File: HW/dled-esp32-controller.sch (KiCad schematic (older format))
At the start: 40 parts, among them J1 PinsI2C, J2 PinsDbg, J3 BootBtn, J4 swRes, J5 LEDcmd, J6 PinsExt, J7 PinsExt2, J8 LEDpwr, J9 Power5V, Q1 STD46P4LLF6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

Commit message: Updates components to add manufacturer, part number, ... fields, checked the values and adds power flags for a clean ERC test
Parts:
- C1, C2, C4, C5, C6, C9: symbol Device:C -> calin:C; characteristics (none) -> 100 nF / 50V / X7R; manufacturer (none) -> Samsung; package (none) -> 0805; part-number (none) -> CL21B104KBCNNNC
- C3: symbol Device:C -> calin:C; characteristics (none) -> 10 µF / 6,3 V; manufacturer (none) -> Samsung; package (none) -> 0805; part-number (none) -> CL21B106KQQNNNE
- C7: value 10uF -> 10uF/10V/1mOhm; symbol Device:C -> calin:C; characteristics (none) -> 10 µF / 16 V / X7R / ESR: 1 mΩ; manufacturer (none) -> Taiyo Yuden; package (none) -> 0805; part-number (none) -> EMK212BB7106KG-T
- C8: value 22uF 1mOhm -> 22uF/6.3V/1mOhm; symbol Device:C -> calin:C; characteristics (none) -> 22 µF / 6.3 V / X5R / ESR: 1 mΩ; manufacturer (none) -> Taiyo Yuden; package (none) -> 0805; part-number (none) -> JMK212BJ226MG-T
- D1: characteristics (none) -> *; manufacturer (none) -> Optoflash; package (none) -> 1206; part-number (none) -> OF-SMD3216B
- H1, H2: characteristics (none) -> *; manufacturer (none) -> pcb; part-number (none) -> DNP
- J1: value PinsI2C -> CS_4
- J2: value PinsDbg -> CS_3
- J3: value BootBtn -> CS_2
- J4: value swRes -> CS_2
- J5: value LEDcmd -> CS_3
- J6: value PinsExt -> CS_5; part-number (none) -> DNP
- J7: value PinsExt2 -> CS_3; part-number (none) -> DNP
- J8: value LEDpwr -> CS_Pwr
- J9: value Power5V -> CS_Pwr; symbol calin:CS_2pwr -> calin:CS_2
- L1: characteristics (none) -> 2.2 uH DCR: 35 mΩ; manufacturer (none) -> Abracon Corporation; package (none) -> *; part-number (none) -> ASPI-0530HI-2R2M-T2
- Q1: characteristics (none) -> *; manufacturer (none) -> STMicroelectronics; package (none) -> DPAK (TO-252); part-number (none) -> STD46P4LLF6
- Q2: characteristics (none) -> *; manufacturer (none) -> International Rectifier; package (none) -> SOT23-3; part-number (none) -> IRLML2502GPbF
- R1: characteristics (none) -> *; manufacturer (none) -> Vishay; package (none) -> 0805; part-number (none) -> CRCW080510K0FKEA
- R10, R2, R5, R9: characteristics (none) -> *; manufacturer (none) -> Vishay; package (none) -> 0805; part-number (none) -> CRCW0805330RFKTABC
- R3, R4: value 2K2 -> 2k2; characteristics (none) -> 2K; manufacturer (none) -> Panasonic; package (none) -> 0805; part-number (none) -> ERJ6ENF2001V
- R6: characteristics (none) -> 442Kohms 1%; manufacturer (none) -> Panasonic; package (none) -> 0805; part-number (none) -> ERJ-6ENF4423V
- R7: characteristics (none) -> 100Kohms 1%; manufacturer (none) -> Panasonic; package (none) -> 0805; part-number (none) -> ERJ-6ENF1003V
- R8: value 10K -> 10k; characteristics (none) -> *; manufacturer (none) -> Vishay; package (none) -> 0805; part-number (none) -> CRCW080510K0FKEA
- SYM1: manufacturer (none) -> pcb; part-number (none) -> DNP
- U1: characteristics (none) -> *; manufacturer (none) -> Espressif; package (none) -> *; part-number (none) -> ESP32-WROOM-32
- U2: characteristics (none) -> Standard CMOS Voltage Detector IC - Open Drain; manufacturer (none) -> ROHM Semiconductor; package (none) -> SSOP3 (SOT23-3); part-number (none) -> BD48K
- U3: characteristics (none) -> Step-Down Converter 2A 1.5MHz Iq=35uA; manufacturer (none) -> Texas Instruments; package (none) -> SOT23-5; part-number (none) -> TLV62569DBV
- U4, U5: characteristics (none) -> Single Power Supply Single Buffer GATE CMOS Logic Level Shi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; manufacturer (none) -> Texas Instruments; package (none) -> SOT23-5; part-number (none) -> SN74LV1T34DBVR
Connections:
- wire segments 126 -> 133
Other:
- moved on the sheet: C6, C7

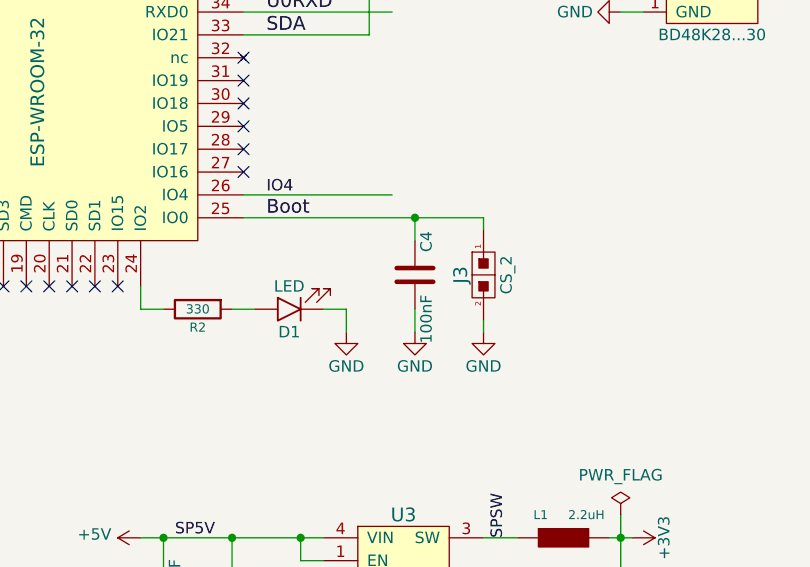
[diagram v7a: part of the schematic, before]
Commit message: Changes the C4 to NC and removes the keepout areas from under ESP32 module, as in Espressif's DevKitC v4
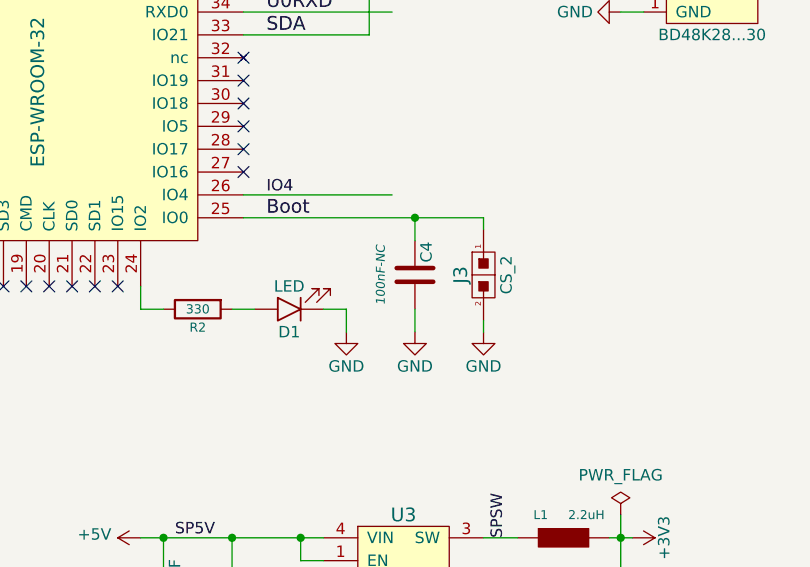
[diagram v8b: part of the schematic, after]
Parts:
- C4: value 100nF -> 100nF-NC; characteristics 100 nF / 50V / X7R -> *; manufacturer Samsung -> (none); part-number CL21B104KBCNNNC -> DNP
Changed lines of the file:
@@
 Sheet 1 1
 Title "dled-esp32-controller"
-Date "2019-04-30"
-Rev "14"
+Date "2019-05-01"
+Rev "15"
 Comp "Calin Radoni"
 Comment1 "https://github.com/CalinRadoni/dled-esp32-controller"
@@
 U 1 1 5B37F59B
 P 5650 3150
-F 0 "C4" V 5700 3250 50  0000 L CNN
-F 1 "100nF" V 5700 2850 50  0000 L CNN
+F 0 "C4" V 5700 3250 50  0000 C CNN
+F 1 "100nF-NC" V 5500 3150 39  0000 C CIN
 F 2 "CalinGeneric:C0805HS" H 5688 3000 50  0001 C CNN
 F 3 "" H 5650 3150 50  0000 C CNN
-F 4 "100 nF / 50V / X7R" H 0   0   50  0001 C CNN "characteristics"
-F 5 "Samsung" H 0   0   50  0001 C CNN "manufacturer"
+F 4 "*" H 0   0   50  0001 C CNN "characteristics"
+F 5 "" H 0   0   50  0001 C CNN "manufacturer"
 F 6 "0805" H 0   0   50  0001 C CNN "package"
-F 7 "CL21B104KBCNNNC" H 0   0   50  0001 C CNN "part-number"
+F 7 "DNP" H 0   0   50  0001 C CNN "part-number"
 	1    5650 3150
 	1    0    0    -1
